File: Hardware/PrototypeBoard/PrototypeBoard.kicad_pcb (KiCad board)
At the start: 4 copper layers, 100 x 60 mm, 141 parts, among them J1 Conn_01x03, J2 Conn_01x06, J3 ControlSupplyConnector, Q1 Q_NMOS_SGD, Q2 Q_NMOS_SGD, Q3 Q_NMOS_SGD, Q4 Q_NMOS_SGD, Q5 Q_NMOS_SGD, Q6 Q_NMOS_SGD, U1 TLI4970-D025T4, U2 TLI4970-D025T4, U3 TLI4970-D025T4, U4 TLE7185-1E, U5 ADC124S021

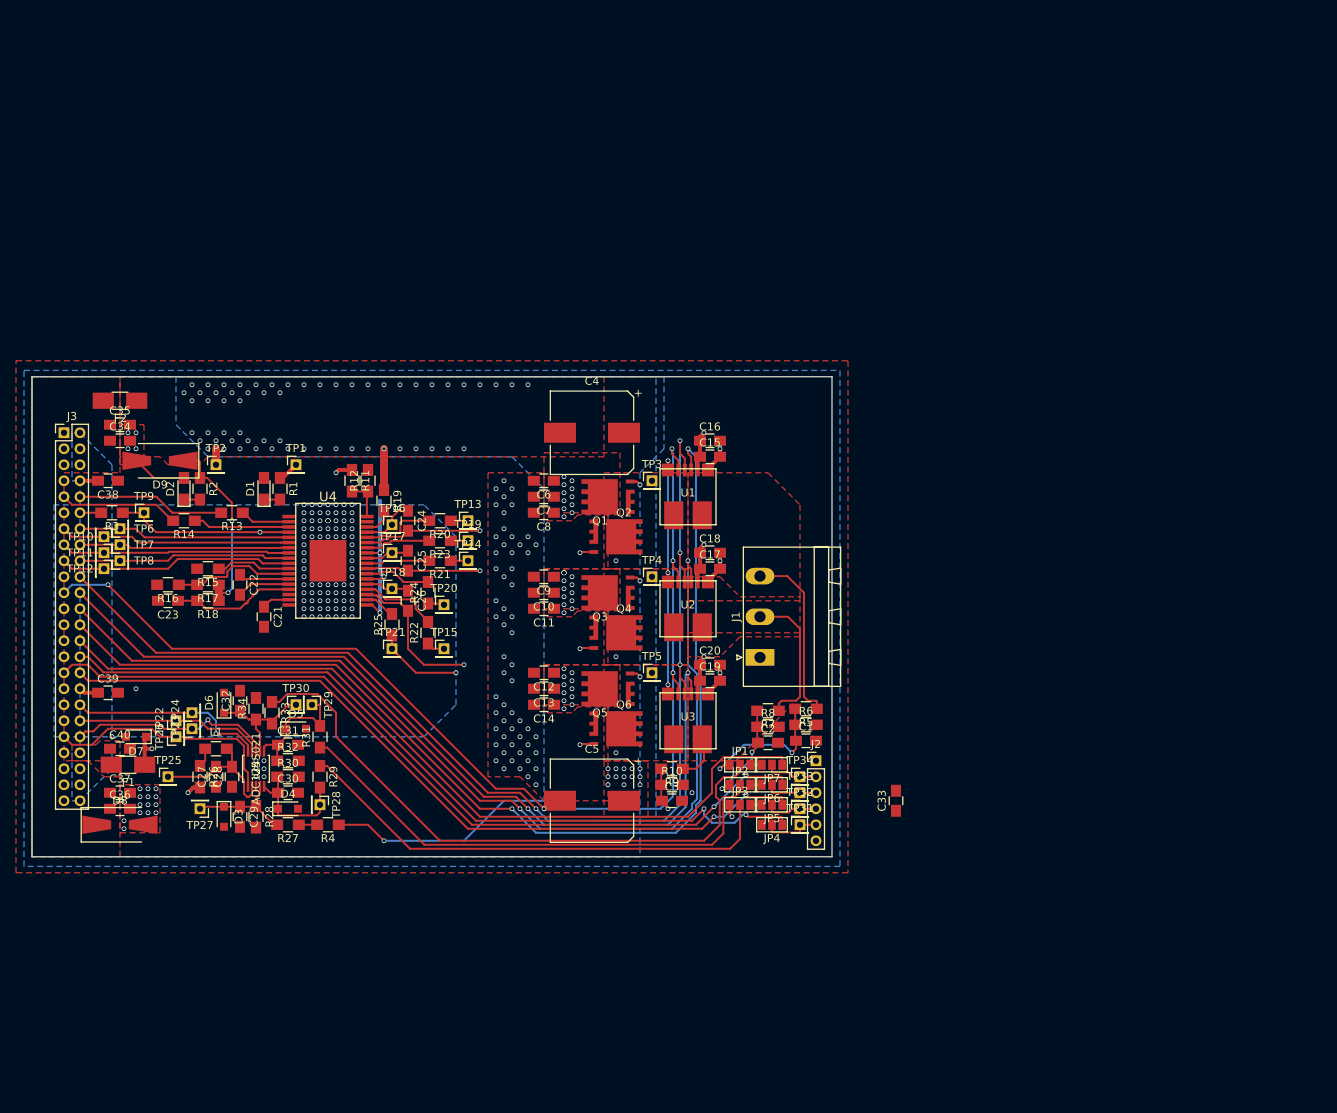
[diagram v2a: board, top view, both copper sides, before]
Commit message: New, much bigger pcb layout, changes to connection PGND <-> GND
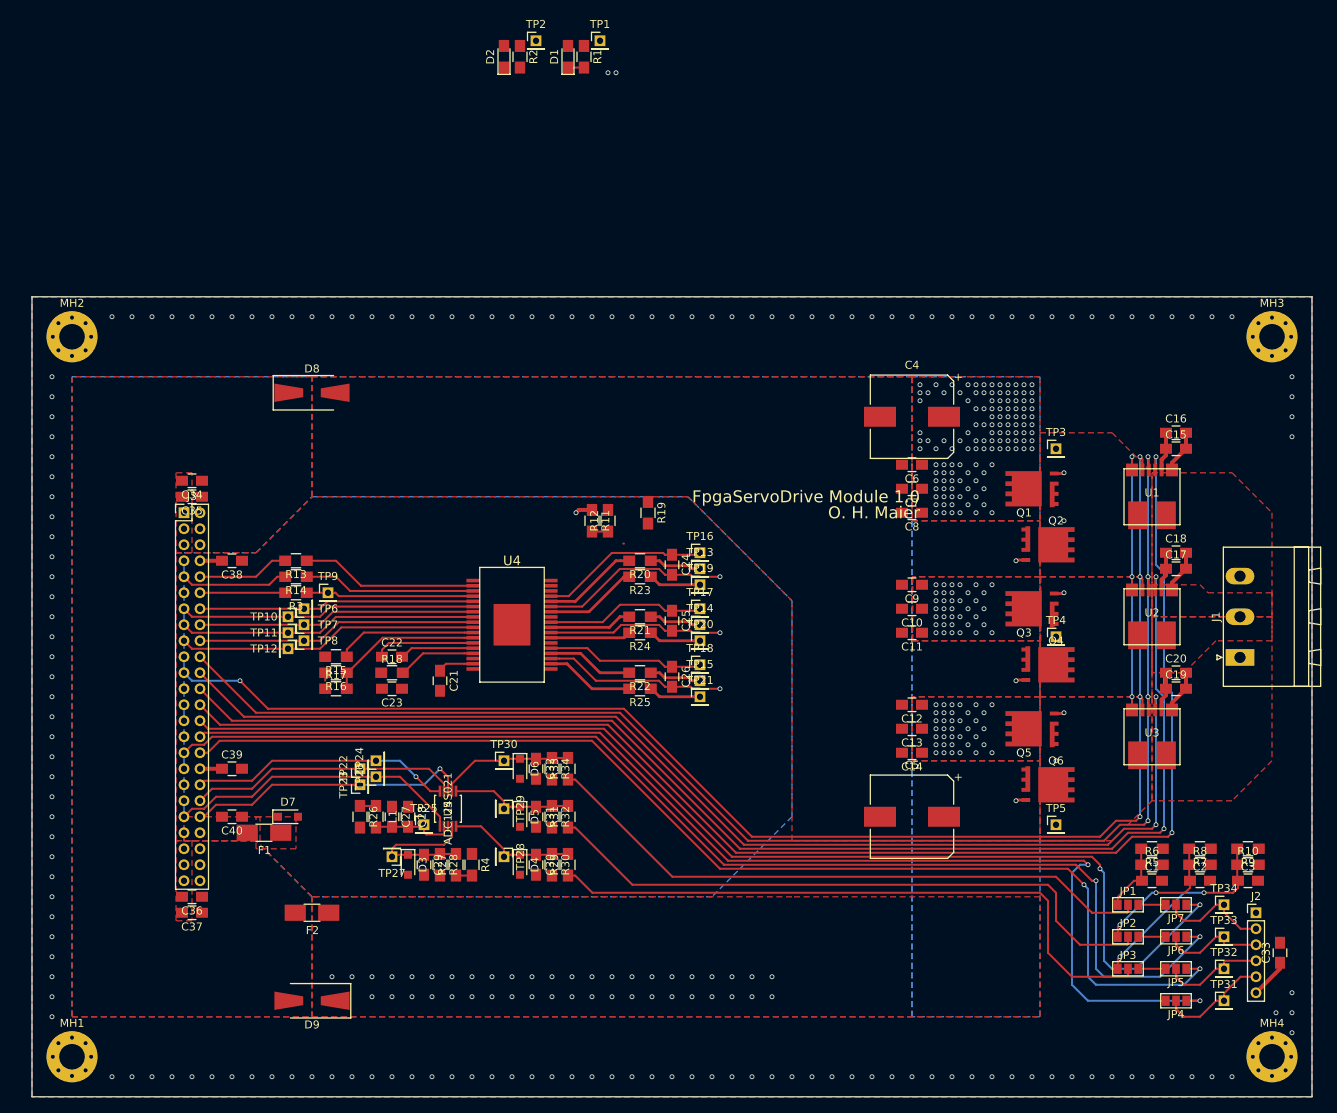
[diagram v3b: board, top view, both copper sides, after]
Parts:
- added MH1: MountingHole_Pad, Mounting_Holes:MountingHole_3.2mm_M3_Pad_Via, F.Cu at (35.0, 115.0)
- added MH2: MountingHole_Pad, Mounting_Holes:MountingHole_3.2mm_M3_Pad_Via, F.Cu at (35.0, 25.0)
- added MH3: MountingHole_Pad, Mounting_Holes:MountingHole_3.2mm_M3_Pad_Via, F.Cu at (185.0, 25.0)
- added MH4: MountingHole_Pad, Mounting_Holes:MountingHole_3.2mm_M3_Pad_Via, F.Cu at (185.0, 115.0)
- moved C3 72.7 mm to (182.0, 93.0)
- moved R10 72.7 mm to (182.0, 91.0)
- moved R9 72.7 mm to (182.0, 89.0)
- moved D9 70.1 mm to (65.0, 108.0)
- moved F2 68.4 mm to (65.0, 97.0)
- moved D2 67.2 mm to (89.0, -10.0)
- moved R2 67.2 mm to (91.0, -10.0)
- moved TP2 66.4 mm to (93.0, -12.0)
- moved D1 66.0 mm to (97.0, -10.0)
- moved R1 66.0 mm to (99.0, -10.0)
- moved TP1 65.2 mm to (101.0, -12.0)
- moved J1 60.0 mm to (181.0, 65.1)
- moved D8 59.1 mm to (65.0, 32.0)
- moved C15 58.3 mm to (173.0, 39.0)
- moved C16 58.3 mm to (173.0, 37.0)
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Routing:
- net /MotorModule/GateDriver/Logic_GD_ENA: track 124.8 -> 55.9 mm, vias 4 -> 3
- net +BATT: track 60.7 -> 0.00 mm
- net /MainConnector/EncoderSpiMiso: track 99.5 -> 153.0 mm
- net /MainConnector/EncoderSpiMosi: track 98.6 -> 147.3 mm
- net /MainConnector/~EncoderSpiCs: track 102.1 -> 150.5 mm
- net /MainConnector/EncoderSpiSclk: track 102.6 -> 149.6 mm, vias 0 -> 2
- net /MainConnector/CurrentSensSpiDoutU: track 138.0 -> 179.7 mm
- net /MainConnector/CurrentSensSpiDoutV: track 123.5 -> 163.4 mm
- net /MainConnector/CurrentSensSpiDoutW: track 108.4 -> 147.1 mm
- net /MainConnector/~CurrentSensSpiCs: track 141.1 -> 179.3 mm
- net /MainConnector/CurrentSensSpiSclk: track 145.7 -> 179.7 mm
- net /MotorModule/CurrentSensing/Power_Phase_U: track 37.3 -> 69.4 mm, vias 3 -> 2
- net /MotorModule/CurrentSensing/Power_Phase_V: track 35.5 -> 66.2 mm, vias 2 -> 1
- net GNDPWR: track 27.1 -> 0.00 mm, vias 77 -> 44
- net /MotorModule/GateDriver/Gate_V_H: track 30.1 -> 56.6 mm
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- added copper zone on F.Cu, net +3V3
- added copper zone on In1.Cu, net +BATT
- removed copper zone on B.Cu, net /MainConnector/PowerIn
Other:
- board size 100 x 60 mm -> 160 x 100 mm
- net class Gate Driver Outputs added: clearance 0.2, trace_width 0.35, via_dia 0.6, via_drill 0.4
- rule trace_min: 0.2 -> 0.09
- rule via_min_drill: 0.3 -> 0.2
- rule via_min_size: 0.4 -> 0.45
- board text added: "FpgaServoDrive Module 1.0"
- board text added: "O. H. Maier"

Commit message: continued to work on new layout
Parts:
- added NT1: Net-Tie_2, NetTie:NetTie-2_SMD_Pad0.5mm, F.Cu at (115.0, 57.5)
- added NT2: Net-Tie_2, NetTie:NetTie-2_SMD_Pad0.5mm, F.Cu at (115.0, 64.5)
- added NT3: Net-Tie_2, NetTie:NetTie-2_SMD_Pad0.5mm, F.Cu at (115.0, 71.5)
- moved D2 62.0 mm to (70.0, 49.0)
- moved R2 62.0 mm to (72.0, 49.0)
- moved TP2 62.0 mm to (74.0, 47.0)
- moved D1 61.7 mm to (79.0, 49.0)
- moved R1 61.7 mm to (81.0, 49.0)
- moved TP1 61.7 mm to (83.0, 47.0)
- moved R19 8.94 mm to (99.0, 51.0)
- moved R11 5.83 mm to (95.0, 51.0)
- moved R12 5.83 mm to (97.0, 51.0)
- moved D7 1.25 mm to (62.8, 84.0)
- moved R23 0.50 mm to (106.0, 55.5)
- moved R24 0.50 mm to (106.0, 62.5)
- moved R25 0.50 mm to (106.0, 69.5)
- moved TP19 0.50 mm to (113.5, 56.5)
- moved TP20 0.50 mm to (113.5, 63.5)
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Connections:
- U4 pad 19: GNDPWR -> GND
- U4 pad 24: GNDPWR -> GND
- U4 pad 29: GNDPWR -> GND
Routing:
- net /MotorModule/CurrentSensing/Power_Phase_U_measured: track 0.00 -> 40.2 mm, vias 0 -> 1
- net /MotorModule/CurrentSensing/Power_Phase_V_measured: track 0.00 -> 33.6 mm, vias 0 -> 1
- net /MotorModule/CurrentSensing/Power_Phase_W_measured: track 0.00 -> 30.2 mm, vias 0 -> 1
- net GNDPWR: track 0.00 -> 29.2 mm, vias 44 -> 46
- net +BATT: track 0.00 -> 7.71 mm, vias 111 -> 134
- net Net-(R19-Pad2): track 0.00 -> 6.77 mm
- net /MotorModule/GateDriver/Gate_W_H: track 55.0 -> 60.0 mm
- net Net-(R11-Pad2): track 2.00 -> 5.18 mm
- net Net-(C23-Pad1): track 9.79 -> 11.8 mm
- net Net-(D1-Pad1): track 2.00 -> 0.00 mm
- net /MainConnector/CurrentSensSpiSclk: track 179.7 -> 181.4 mm, vias 4 -> 5
- net /MainConnector/CurrentSensSpiDoutW: track 147.1 -> 148.8 mm, vias 2 -> 3
- net /MainConnector/CurrentSensSpiDoutU: track 179.7 -> 181.4 mm, vias 2 -> 3
- net /MainConnector/~CurrentSensSpiCs: track 179.3 -> 181.0 mm, vias 5 -> 6
- net /MainConnector/CurrentSensSpiDoutV: track 163.4 -> 165.1 mm, vias 2 -> 3
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- added copper zone on In2.Cu, net +3V3
- added copper zone on In2.Cu, net +BATT
- added copper zone on In2.Cu, net /MainConnector/3V3in
- added copper zone on In1.Cu, net GND
- removed copper zone on In1.Cu, net +3V3
- removed copper zone on In1.Cu, net +BATT
- removed copper zone on In1.Cu, net /MainConnector/3V3in
- removed copper zone on In1.Cu, net /MainConnector/PowerIn
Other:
- net class Gate Driver Outputs: trace_width 0.35 -> 0.4

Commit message: New layout almost complete
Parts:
- moved F2 42.7 mm to (100.0, 121.5)
- moved NT1 40.9 mm to (150.5, 77.8)
- moved NT2 40.9 mm to (150.5, 84.8)
- moved NT3 40.9 mm to (150.5, 91.8)
- moved C1 40.3 mm to (205.0, 113.0)
- moved C10 40.3 mm to (175.0, 79.0)
- moved C11 40.3 mm to (175.0, 82.0)
- moved C12 40.3 mm to (175.0, 91.0)
- moved C13 40.3 mm to (175.0, 94.0)
- moved C14 40.3 mm to (175.0, 97.0)
- moved C15 40.3 mm to (208.0, 59.0)
- moved C16 40.3 mm to (208.0, 57.0)
- moved C17 40.3 mm to (208.0, 74.0)
- moved C18 40.3 mm to (208.0, 72.0)
- moved C19 40.3 mm to (208.0, 89.0)
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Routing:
- net +BATT: track 7.71 -> 109.0 mm, vias 134 -> 308
- net /MotorModule/GateDriver/Logic_GD_ENA: track 55.9 -> 141.7 mm, vias 3 -> 4
- net +3V3: track 22.8 -> 27.1 mm, vias 11 -> 12
- net GNDPWR: track 29.2 -> 32.9 mm, vias 46 -> 101
- net /MainConnector/EncoderSpiMiso: track 153.0 -> 151.0 mm
- net Net-(D2-Pad1): track 0.00 -> 2.00 mm
- net Net-(D1-Pad1): track 0.00 -> 2.00 mm
- net /MainConnector/AdcSpiMosi: track 35.7 -> 37.5 mm
- net GND: track 17.0 -> 18.7 mm
- net /MotorModule/CurrentSensing/Power_Phase_W_measured: track 30.2 -> 28.7 mm
- net /MotorModule/CurrentSensing/Power_Phase_V_measured: track 33.6 -> 32.5 mm
- net /MotorModule/GateDriver/Gate_W_H: track 60.0 -> 60.8 mm
- net /MotorModule/CurrentSensing/Power_Phase_W: track 69.0 -> 69.9 mm
- net /MainConnector/EncoderSpiMosi: track 147.3 -> 146.7 mm
- net (no net): vias 16 -> 10
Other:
- board text added: "09/2018 O. H. Maier"
- board text added: "ADC"
- board text added: "Encoder"
- board text added: "FpgaServoDrive"
- board text added: "Gate Driver"
- board text added: "Phase Current Measurement"
- board text added: "Power Stage"
- board text added: "Prototype Module 1.0"
- board text removed: "FpgaServoDrive Module 1.0"
- board text removed: "O. H. Maier"

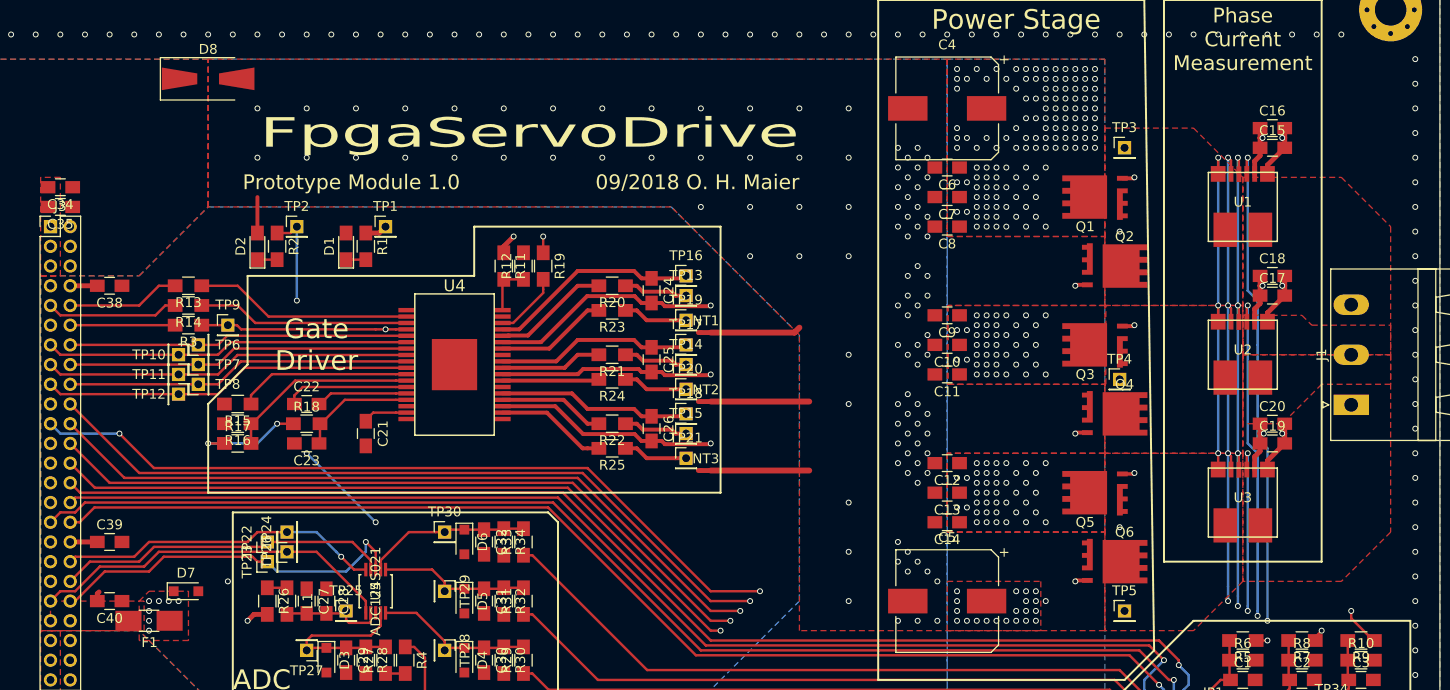
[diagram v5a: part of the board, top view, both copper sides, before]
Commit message: Gate driver closer to power stage, ground and power ground seperated completely, power ground traces to gate driver replaced by power planes, phase outputs now span across all layers (vias not places yet)
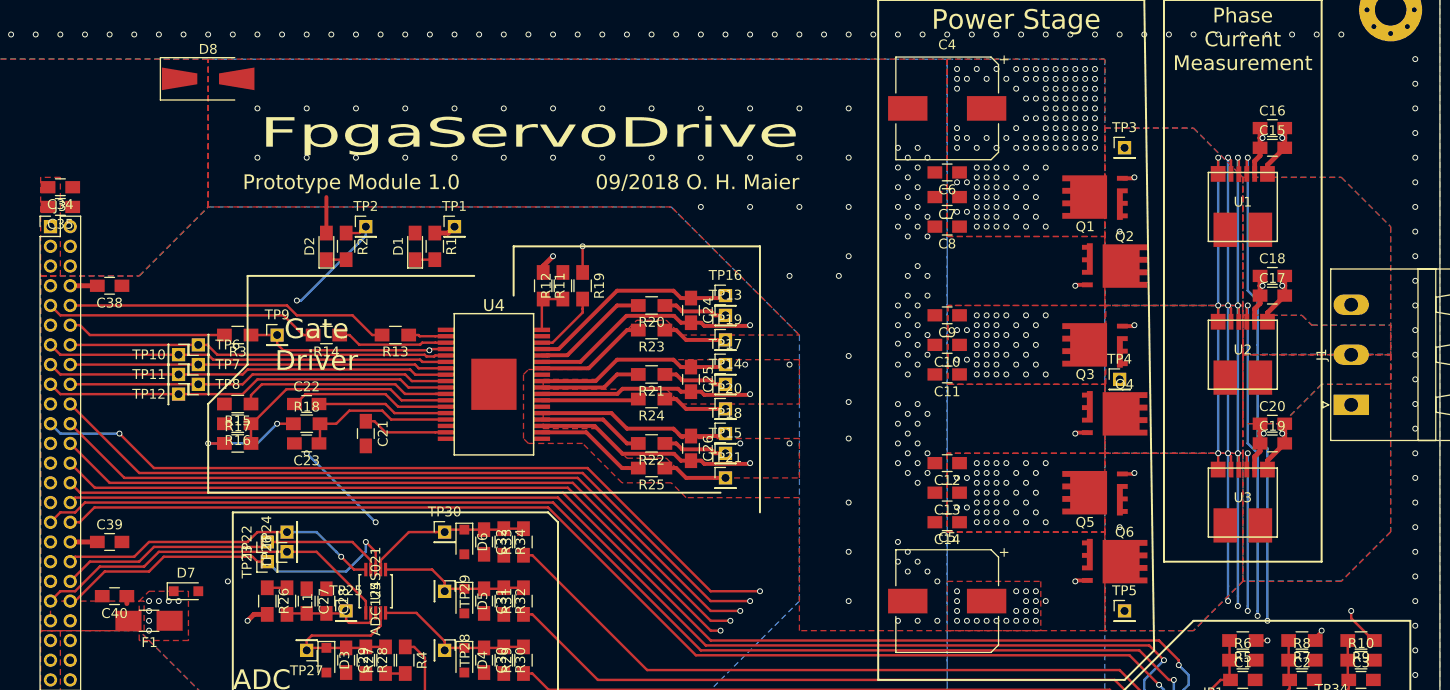
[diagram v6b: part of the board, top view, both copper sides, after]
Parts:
- removed NT1, NT2, NT3: Net-Tie_2, NetTie:NetTie-2_SMD_Pad0.5mm
- moved R13 21.6 mm to (119.0, 78.0)
- moved R14 14.3 mm to (112.0, 78.0)
- moved D1 7.00 mm to (121.0, 69.0)
- moved D2 7.00 mm to (112.0, 69.0)
- moved R1 7.00 mm to (123.0, 69.0)
- moved R2 7.00 mm to (114.0, 69.0)
- moved TP1 7.00 mm to (125.0, 67.0)
- moved TP2 7.00 mm to (116.0, 67.0)
- moved R3 5.10 mm to (103.0, 78.0)
- moved TP9 5.10 mm to (107.0, 78.0)
- moved C24 4.47 mm to (149.0, 75.5)
- moved C25 4.47 mm to (149.0, 82.5)
- moved C26 4.47 mm to (149.0, 89.5)
- moved R11 4.47 mm to (134.0, 73.0)
- moved R12 4.47 mm to (136.0, 73.0)
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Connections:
- U4 pad 19: GND -> GNDPWR
- U4 pad 24: GND -> GNDPWR
- U4 pad 29: GND -> GNDPWR
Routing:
- net GNDPWR: track 32.9 -> 3.65 mm, vias 101 -> 102
- net /MainConnector/~GateDriverErr2: track 11.5 -> 32.9 mm
- net Net-(R13-Pad1): track 22.1 -> 3.84 mm
- net /MainConnector/~GateDriverErr1: track 13.5 -> 27.9 mm
- net Net-(R14-Pad1): track 21.5 -> 11.3 mm
- net /MotorModule/GateDriver/Gate_V_H: track 57.5 -> 51.8 mm
- net /MotorModule/CurrentSensing/Power_Phase_V: track 66.3 -> 60.7 mm
- net /MainConnector/GateDriverEna: track 10.7 -> 16.1 mm
- net Net-(R15-Pad1): track 17.6 -> 22.6 mm
- net /MotorModule/GateDriver/Gate_W_L: track 52.5 -> 47.7 mm
- net /MotorModule/GateDriver/Gate_W_H: track 60.8 -> 56.0 mm
- net /MotorModule/GateDriver/Gate_V_L: track 49.2 -> 44.4 mm
- net /MotorModule/CurrentSensing/Power_Phase_W: track 69.9 -> 65.0 mm
- net /MainConnector/~PwmUH: track 34.5 -> 38.7 mm
- net Net-(R16-Pad1): track 19.6 -> 23.7 mm
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- added copper zone on B.Cu, net /MotorModule/CurrentSensing/Power_Phase_U
- added copper zone on In1.Cu, net /MotorModule/CurrentSensing/Power_Phase_U
- added copper zone on In2.Cu, net /MotorModule/CurrentSensing/Power_Phase_U
- added copper zone on B.Cu, net /MotorModule/CurrentSensing/Power_Phase_U_measured
- added copper zone on In1.Cu, net /MotorModule/CurrentSensing/Power_Phase_U_measured
- added copper zone on In2.Cu, net /MotorModule/CurrentSensing/Power_Phase_U_measured
- added copper zone on B.Cu, net /MotorModule/CurrentSensing/Power_Phase_V
- added copper zone on In1.Cu, net /MotorModule/CurrentSensing/Power_Phase_V
- added copper zone on In2.Cu, net /MotorModule/CurrentSensing/Power_Phase_V
- added copper zone on B.Cu, net /MotorModule/CurrentSensing/Power_Phase_V_measured
- added copper zone on In1.Cu, net /MotorModule/CurrentSensing/Power_Phase_V_measured
- added copper zone on In2.Cu, net /MotorModule/CurrentSensing/Power_Phase_V_measured
- added copper zone on B.Cu, net /MotorModule/CurrentSensing/Power_Phase_W
- added copper zone on In1.Cu, net /MotorModule/CurrentSensing/Power_Phase_W
- added copper zone on In2.Cu, net /MotorModule/CurrentSensing/Power_Phase_W
- added copper zone on B.Cu, net /MotorModule/CurrentSensing/Power_Phase_W_measured
- added copper zone on In1.Cu, net /MotorModule/CurrentSensing/Power_Phase_W_measured
- added copper zone on In2.Cu, net /MotorModule/CurrentSensing/Power_Phase_W_measured
